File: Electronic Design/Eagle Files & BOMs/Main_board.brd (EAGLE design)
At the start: 99.9 x 67.9 mm, 36 parts, among them IC1 ACS712ELC-5A, IC2 ATMEGA328-PU, Q1 IRF9540, Q2 IRF9540, X1 16MHz

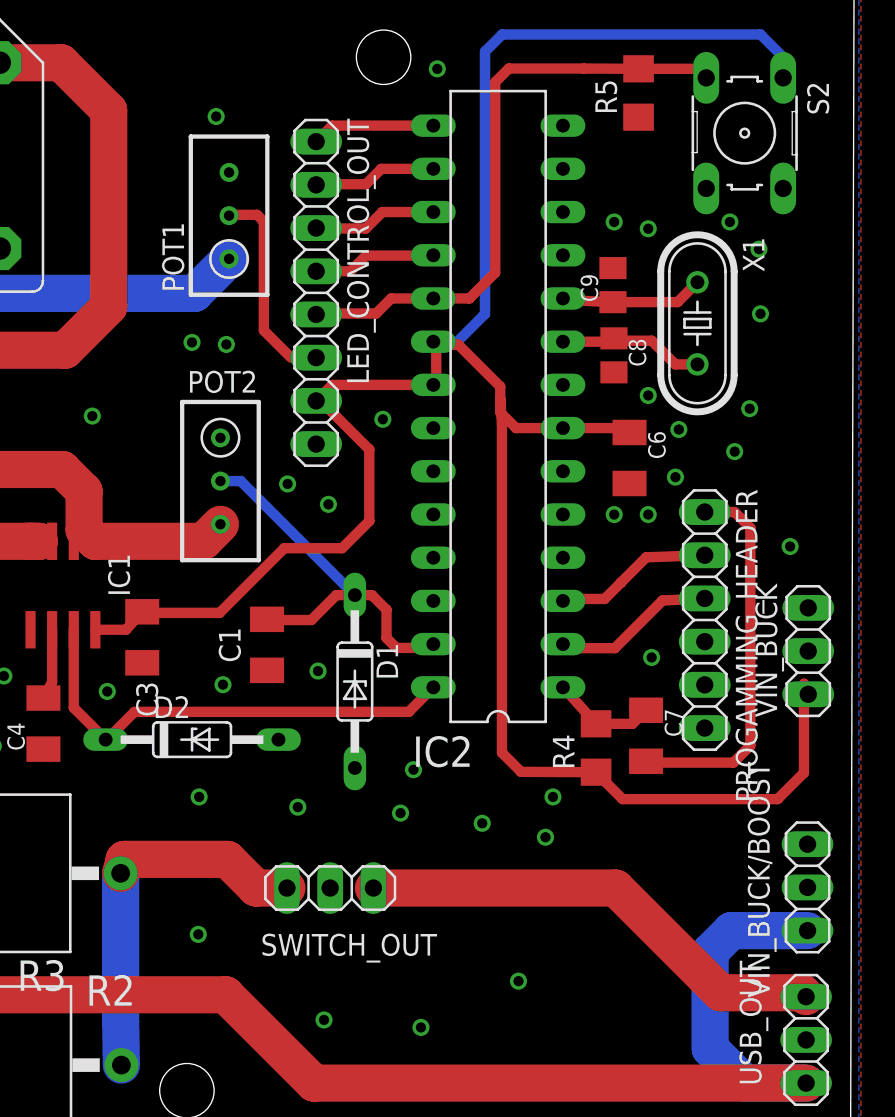
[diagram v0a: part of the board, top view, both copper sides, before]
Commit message: adding breakout for atmega analog pins
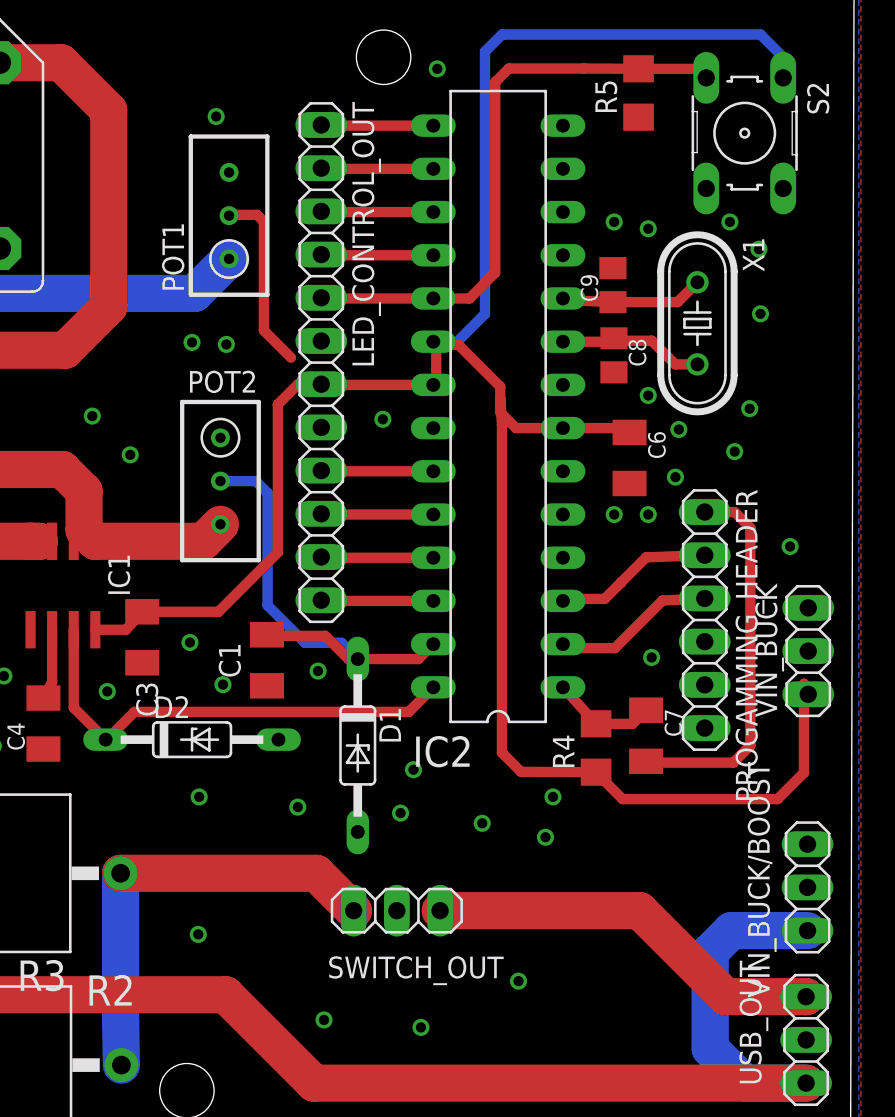
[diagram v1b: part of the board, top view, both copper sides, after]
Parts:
- LED_CONTROL_OUT: device pinhead:1X08 -> pinhead:1X12
- moved SWITCH_OUT 4.14 mm to (73.0, 14.1)
- moved LED_CONTROL_OUT 4.11 mm to (68.6, 46.3)
- moved D1 3.76 mm to (70.7, 23.8)
- moved C1 0.91 mm to (65.4, 28.8)
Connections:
- new net ANALOG_0: IC2.23, LED_CONTROL_OUT.9
- new net ANALOG_1: IC2.24, LED_CONTROL_OUT.10
- new net ANALOG_2: IC2.25, LED_CONTROL_OUT.11
- new net ANALOG_3: IC2.26, LED_CONTROL_OUT.12
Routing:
- net ANALOG_3: track 0.00 -> 6.60 mm
- net ANALOG_2: track 0.00 -> 6.60 mm
- net ANALOG_1: track 0.00 -> 6.60 mm
- net ANALOG_0: track 0.00 -> 6.60 mm
- net N$13: track 28.1 -> 23.6 mm
- net +5V: track 136.9 -> 133.2 mm
- net VIN: track 23.4 -> 27.0 mm
- net N$24: track 22.4 -> 25.9 mm
- net N$11: track 7.30 -> 6.60 mm
- net N$12: track 7.28 -> 6.60 mm
- net N$9: track 7.28 -> 6.60 mm
- net N$8: track 35.7 -> 35.0 mm
- net N$6: track 7.28 -> 6.60 mm

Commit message: redrawing board
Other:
- board size 99.9 x 67.9 mm -> 99.9 x 68 mm
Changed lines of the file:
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@@
 <board>
 <plain>
-<wire x1="0.062675" y1="0.0095125" x2="99.7111375" y2="0.0193875" width="0" layer="20"/>
-<wire x1="99.7111375" y1="0.0193875" x2="99.913640625" y2="67.89416875" width="0" layer="20"/>
+<wire x1="0" y1="0" x2="99.9" y2="0" width="0" layer="20"/>
+<wire x1="99.9" y1="0" x2="99.9" y2="68" width="0" layer="20"/>
 <hole x="3.19508125" y="64.469571875" drill="3.2"/>
 <hole x="72.259146875" y="64.22315" drill="3.2"/>
 <hole x="60.695490625" y="3.4702" drill="3.2"/>
 <hole x="2.85523125" y="2.6960375" drill="3.2"/>
+<wire x1="0" y1="0" x2="0" y2="68" width="0" layer="20"/>
+<wire x1="99.9" y1="68" x2="0" y2="68" width="0" layer="20"/>
 </plain>
 <attributes>

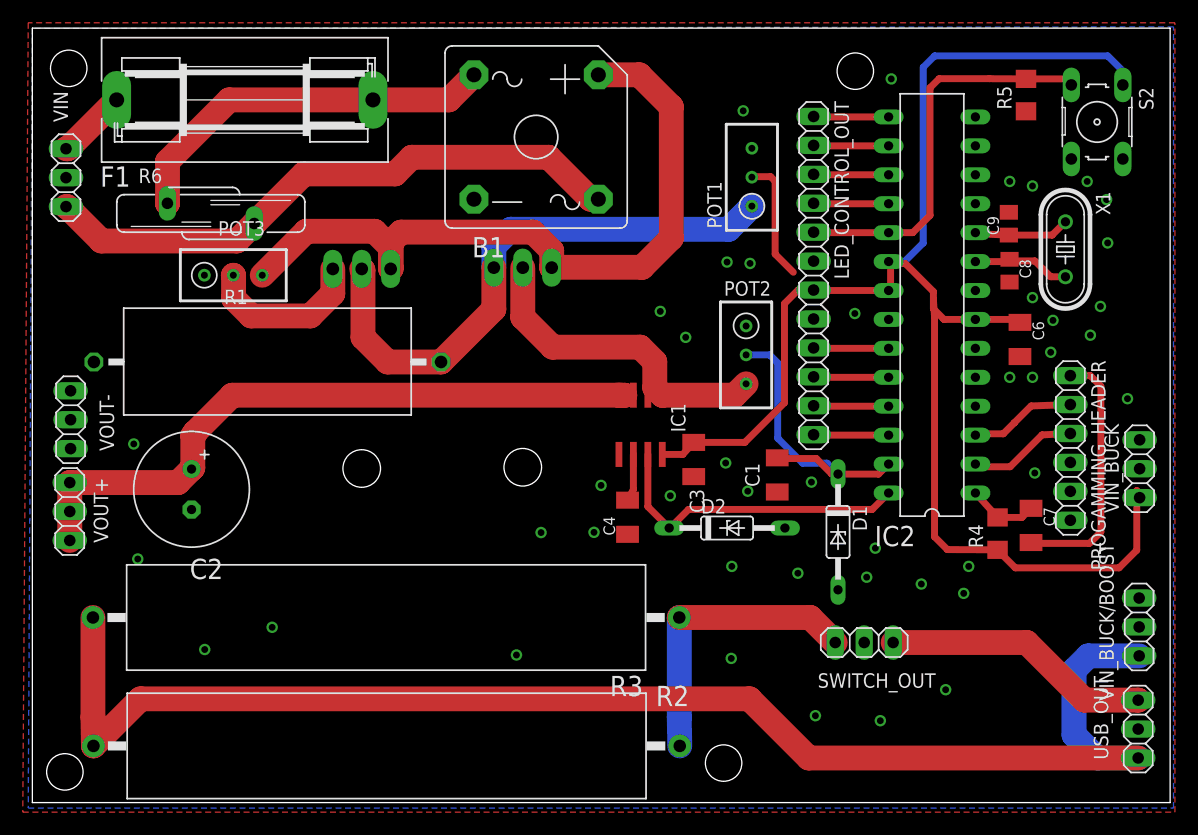
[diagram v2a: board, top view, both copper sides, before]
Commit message: moving terminal outputs into better postions
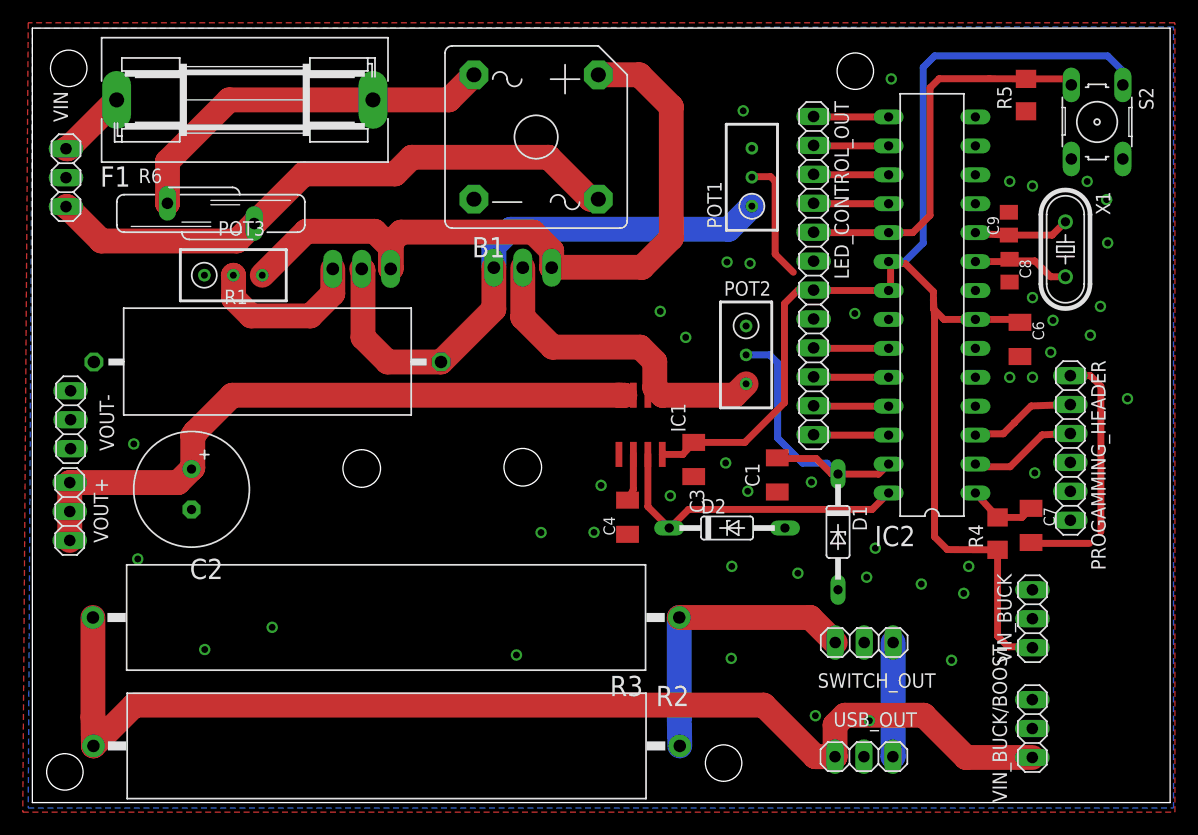
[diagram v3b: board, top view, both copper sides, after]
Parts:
- moved USB_OUT 24.2 mm to (73.0, 4.03), turned to 0 degrees
- moved VIN_BUCK 16.2 mm to (87.8, 16.1)
- moved VIN_BUCK/BOOST 12.9 mm to (87.8, 6.50)
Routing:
- net N$23: track 125.3 -> 101.7 mm
- net N$13: track 23.6 -> 10.0 mm
- net +5V: track 133.2 -> 124.9 mm
- net N$14: track 22.4 -> 21.0 mm
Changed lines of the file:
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@@
 <attribute name="VALUE" x="6.53230625" y="29.8068625" size="1.27" layer="27" rot="R90"/>
 </element>
-<element name="VIN_BUCK" library="pinhead" package="1X03" value="" x="97.22119375" y="29.314190625" rot="R90"/>
+<element name="VIN_BUCK" library="pinhead" package="1X03" value="" x="87.81119375" y="16.144190625" rot="R90"/>
 <element name="PROGAMMING_HEADER" library="pinhead" package="1X06" value="" x="91.138590625" y="31.138721875" rot="R270"/>
 <element name="C6" library="resistor" package="C1206K" value="10u" x="86.71648125" y="40.66599375" rot="R270"/>
-<element name="VIN_BUCK/BOOST" library="pinhead" package="1X03" value="" x="97.1813125" y="15.42156875" smashed="yes" rot="R90">
-<attribute name="NAME" x="94.9525125" y="8.93536875" size="1.27" layer="25" ratio="10" rot="R90"/>
-<attribute name="VALUE" x="100.3563125" y="11.61156875" size="1.27" layer="27" rot="R90"/>
+<element name="VIN_BUCK/BOOST" library="pinhead" package="1X03" value="" x="87.8013125" y="6.50156875" smashed="yes" rot="R90">
+<attribute name="NAME" x="85.5725125" y="0.01536875" size="1.27" layer="25" ratio="10" rot="R90"/>
+<attribute name="VALUE" x="90.9763125" y="2.69156875" size="1.27" layer="27" rot="R90"/>
 </element>
 <element name="R2" library="resistor-power" package="RWM8X45" value="22R" x="31.10564375" y="4.9753625" smashed="yes" rot="R180">
@@
 <attribute name="MPN" value="" x="31.06038125" y="16.251775" size="1.778" layer="27" rot="R180" display="off"/>
 </element>
-<element name="USB_OUT" library="pinhead" package="1X03" value="" x="97.095434375" y="6.456034375" smashed="yes" rot="R90">
-<attribute name="NAME" x="94.466634375" y="3.769834375" size="1.27" layer="25" ratio="10" rot="R90"/>
-<attribute name="VALUE" x="100.270434375" y="2.646034375" size="1.27" layer="27" rot="R90"/>
+<element name="USB_OUT" library="pinhead" package="1X03" value="" x="73.016034375" y="4.034565625" smashed="yes">
+<attribute name="NAME" x="70.329834375" y="6.663365625" size="1.27" layer="25" ratio="10"/>
+<attribute name="VALUE" x="69.206034375" y="0.859565625" size="1.27" layer="27"/>
 </element>
 <element name="S2" library="switch-omron" package="B3F-10XX" value="" x="93.486315625" y="59.761790625" rot="R270">
@@
 <via x="57.36569375" y="40.8502" extent="1-16" drill="0.6" shape="square"/>
 <via x="74.01569375" y="22.3402" extent="1-16" drill="0.6" shape="square"/>
-<via x="80.189946875" y="9.911478125" extent="1-16" drill="0.6" shape="square"/>
-<via x="74.45569375" y="7.1902" extent="1-16" drill="0.6" shape="square"/>
+<via x="80.709946875" y="12.491478125" extent="1-16" drill="0.6" shape="square"/>
+<via x="73.49569375" y="7.1902" extent="1-16" drill="0.6" shape="square"/>
 <via x="67.21569375" y="20.1402" extent="1-16" drill="0.6" shape="square"/>
 <via x="21.05569375" y="15.3902" extent="1-16" drill="0.6" shape="square"/>
@@
 <wire x1="76.42" y1="47.329528125" x2="75.3559375" y2="47.329528125" width="0.6096" layer="16"/>
 <wire x1="75.3559375" y1="47.329528125" x2="75.1825375" y2="47.502928125" width="0.6096" layer="16"/>
-<wire x1="84.748209375" y1="22.19436875" x2="84.748209375" y2="22.171790625" width="0.6096" layer="1"/>
-<wire x1="84.748209375" y1="22.171790625" x2="86.31" y2="20.61" width="0.6096" layer="1"/>
-<wire x1="86.31" y1="20.61" x2="95.42" y2="20.61" width="0.6096" layer="1"/>
-<wire x1="95.42" y1="20.61" x2="96.97" y2="22.16" width="0.6096" layer="1"/>
-<wire x1="96.97" y1="22.16" x2="96.97" y2="27.395384375" width="0.6096" layer="1"/>
-<wire x1="96.97" y1="27.395384375" x2="97.22119375" y2="26.774190625" width="0.6096" layer="1"/>
 <wire x1="68.5950375" y1="45.00298125" x2="67.23298125" y2="45.00298125" width="0.6096" layer="1"/>
 <wire x1="67.23298125" y1="45.00298125" x2="66.04" y2="43.81" width="0.6096" layer="1"/>
@@
 <wire x1="62.55475625" y1="31.62475625" x2="66.04" y2="35.11" width="0.6096" layer="1"/>
 <wire x1="66.04" y1="35.11" x2="66.04" y2="43.81" width="0.6096" layer="1"/>
+<wire x1="84.748209375" y1="22.19436875" x2="84.748209375" y2="14.611790625" width="0.6096" layer="1"/>
+<wire x1="84.748209375" y1="14.611790625" x2="85.68" y2="13.68" width="0.6096" layer="1"/>
+<wire x1="85.68" y1="13.68" x2="87.735384375" y2="13.68" width="0.6096" layer="1"/>
+<wire x1="87.735384375" y1="13.68" x2="87.81119375" y2="13.604190625" width="0.6096" layer="1"/>
 </signal>
 <signal name="N$15">
@@
 <wire x1="92.891278125" y1="37.488721875" x2="93.82" y2="36.56" width="0.6096" layer="1"/>
 <wire x1="93.82" y1="36.56" x2="93.82" y2="23.76" width="0.6096" layer="1"/>
-<wire x1="93.82" y1="23.76" x2="92.82" y2="22.76" width="0.6096" layer="1"/>
 <wire x1="92.82" y1="22.76" x2="87.765809375" y2="22.76" width="0.6096" layer="1"/>
 <wire x1="87.765809375" y1="22.76" x2="87.689071875" y2="22.8367375" width="0.6096" layer="1"/>
+<wire x1="92.82" y1="22.76" x2="93.82" y2="23.76" width="0" layer="19" extent="1-1"/>
 </signal>
 <signal name="N$23">
@@
 <wire x1="5.32038125" y1="16.251775" x2="5.32038125" y2="7.4901" width="2.1844" layer="1"/>
 <wire x1="5.32038125" y1="7.4901" x2="5.36564375" y2="4.9753625" width="2.1844" layer="1"/>
-<wire x1="97.095434375" y1="3.916034375" x2="68.163965625" y2="3.916034375" width="2.1844" layer="1"/>
-<wire x1="68.163965625" y1="3.916034375" x2="62.97" y2="9.11" width="2.1844" layer="1"/>
-<wire x1="62.97" y1="9.11" x2="9.50028125" y2="9.11" width="2.1844" layer="1"/>
-<wire x1="9.50028125" y1="9.11" x2="5.36564375" y2="4.9753625" width="2.1844" layer="1"/>
-<wire x1="97.1813125" y1="12.88156875" x2="92.71156875" y2="12.88156875" width="2.1844" layer="16"/>
-<wire x1="92.71156875" y1="12.88156875" x2="91.46" y2="11.63" width="2.1844" layer="16"/>
-<wire x1="91.46" y1="11.63" x2="91.46" y2="5.946034375" width="2.1844" layer="16"/>
-<wire x1="91.46" y1="5.946034375" x2="93.49" y2="3.916034375" width="2.1844" layer="16"/>
-<wire x1="93.49" y1="3.916034375" x2="97.095434375" y2="3.916034375" width="2.1844" layer="16"/>
+<wire x1="87.8013125" y1="3.96156875" x2="81.97843125" y2="3.96156875" width="2.1844" layer="1"/>
+<wire x1="81.97843125" y1="3.96156875" x2="78.27" y2="7.67" width="2.1844" layer="1"/>
+<wire x1="78.27" y1="7.67" x2="71.34" y2="7.67" width="2.1844" layer="1"/>
+<wire x1="71.34" y1="7.67" x2="70.48" y2="6.81" width="2.1844" layer="1"/>
+<wire x1="70.48" y1="6.81" x2="70.48" y2="4.03853125" width="2.1844" layer="1"/>
+<wire x1="70.48" y1="4.03853125" x2="70.476034375" y2="4.034565625" width="2.1844" layer="1"/>
+<wire x1="70.476034375" y1="4.034565625" x2="68.735434375" y2="4.034565625" width="2.1844" layer="1"/>
+<wire x1="68.735434375" y1="4.034565625" x2="64.21" y2="8.56" width="2.1844" layer="1"/>
+<wire x1="64.21" y1="8.56" x2="8.95028125" y2="8.56" width="2.1844" layer="1"/>
+<wire x1="8.95028125" y1="8.56" x2="5.36564375" y2="4.9753625" width="2.1844" layer="1"/>
 </signal>
 <signal name="N$24">
@@
 <contactref element="USB_OUT" pad="3"/>
 <contactref element="SWITCH_OUT" pad="1"/>
-<wire x1="75.578925" y1="14.053903125" x2="87.316096875" y2="14.053903125" width="2.1844" layer="1"/>
-<wire x1="87.316096875" y1="14.053903125" x2="92.37" y2="9" width="2.1844" layer="1"/>
-<wire x1="92.37" y1="9" x2="97.09146875" y2="9" width="2.1844" layer="1"/>
-<wire x1="97.09146875" y1="9" x2="97.095434375" y2="8.996034375" width="2.1844" layer="1"/>
+<wire x1="75.578925" y1="14.053903125" x2="75.578925" y2="4.05745625" width="2.1844" layer="16"/>
+<wire x1="75.578925" y1="4.05745625" x2="75.556034375" y2="4.034565625" width="2.1844" layer="16"/>
 </signal>
 <signal name="N$1">
